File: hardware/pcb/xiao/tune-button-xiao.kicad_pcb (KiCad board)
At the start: 2 copper layers, 46 x 67 mm, 18 parts, among them J1 XIAO left, J2 XIAO right, J3 LiPo, J4 to XIAO BAT, SW1 MX switch, SW2 MX switch, SW3 MX switch, SW4 MX switch

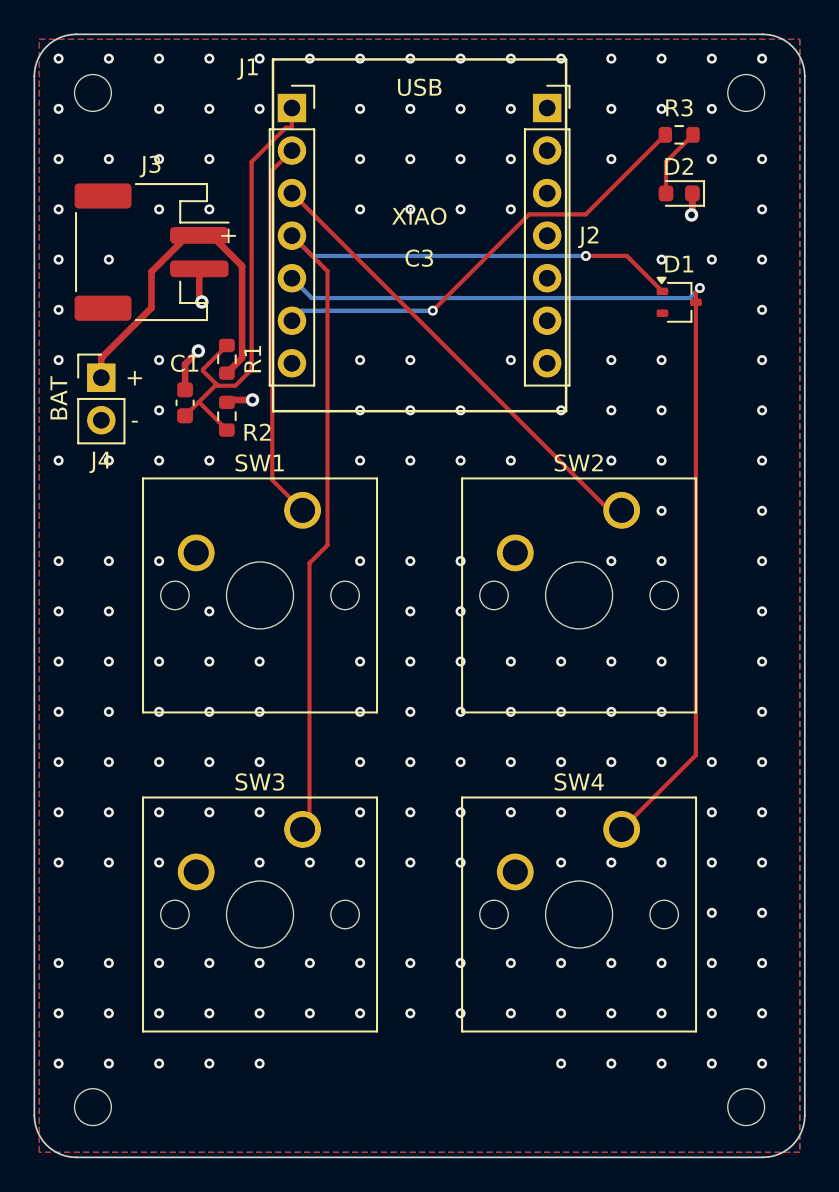
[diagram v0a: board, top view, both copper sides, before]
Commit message: pcb: fixes from the second DFM audit and visual review
- JLC BOM: no designator ranges (KiCad wrote R5-R7, so the CPL lost R5/R6/R7); fab_jlc.py now
  refuses a BOM part with no placement.
- Stitching vias kept off SMD pad openings (two were in the module ground pad's paste).
- Logo drawn as rows at the stroke pitch with caps inset, so gaps keep their size; 15 mm wide.
- Labels only where their own part is the nearest body (R13 and U4 were ambiguous).
- Battery + marks off the pads; USB-C slot paste overprinted 0.2 mm; footprint silk >= 0.15 mm.
- C3 board 70.1 mm long so the USB-C legs clear the switch housings by 0.3 mm.
- Stop tracking __pycache__.
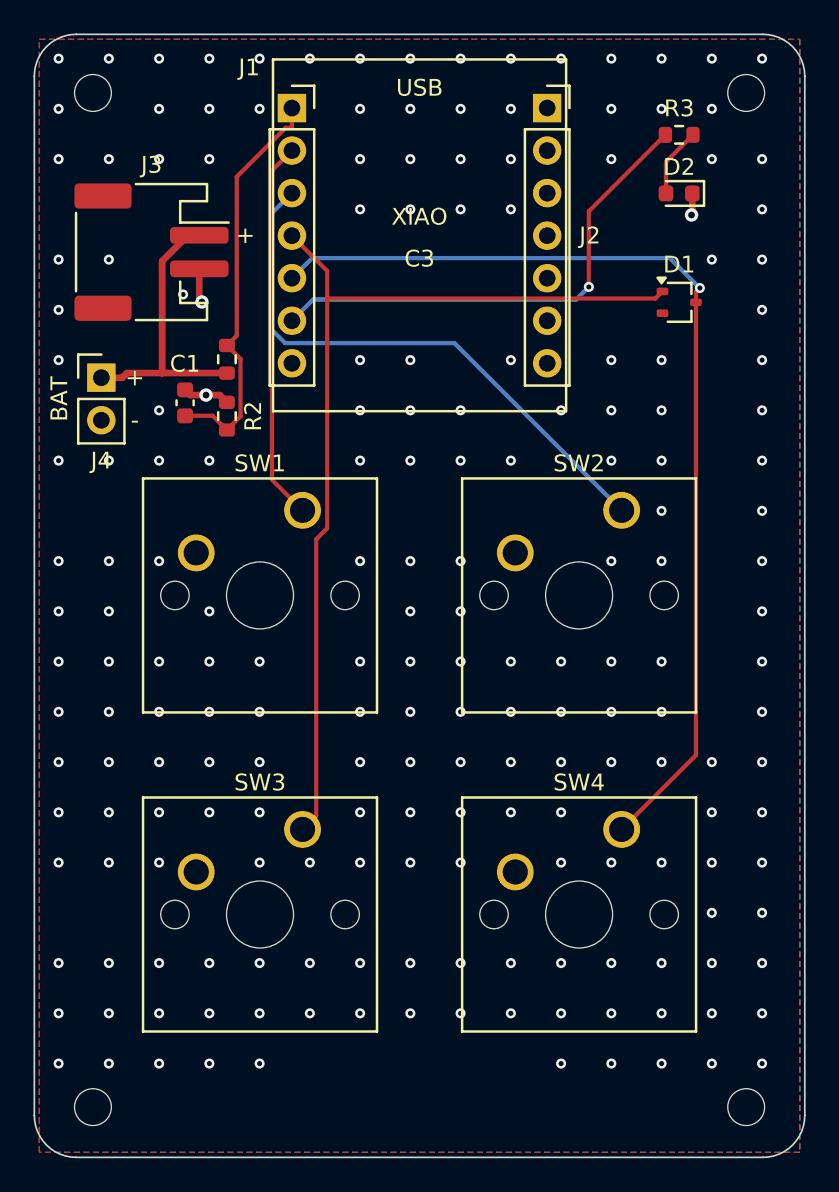
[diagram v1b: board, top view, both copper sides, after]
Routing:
- net K2: track 27.5 -> 34.0 mm
- net VBAT: track 21.4 -> 17.2 mm
- net K3: track 60.4 -> 57.1 mm, vias 1 -> 0
- net VBAT_SENSE: track 27.6 -> 24.6 mm
- net LED: track 26.9 -> 29.5 mm
- net GND: track 7.59 -> 6.16 mm, vias 207 -> 202

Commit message: pcb (c3): fixes from the second simulation pass
- C1 4.7u -> 10u 0805 (C15850, Basic): with R13, plug-in ringing on low-resistance cables peaks
  around 5.6 V instead of 6.1 V (RT9080 absolute max 6.5 V).
- D4, a 1N5819WS across Q1: in the ~3-5 ms after unplugging, before Q1 turns on, the cell feeds
  VSYS through 0.35 V rather than the body diode's 0.6 V, so a Wi-Fi burst there stays above
  brown-out at a 3.4 V cell.
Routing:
- net K3: track 57.1 -> 61.6 mm, vias 0 -> 1
- net LED: track 29.5 -> 27.0 mm
- net GND: track 6.16 -> 7.60 mm, vias 202 -> 211
- net K4: track 59.9 -> 58.7 mm
- net VBAT_SENSE: track 24.6 -> 25.3 mm
- net K1: track 22.7 -> 22.2 mm

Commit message: pcb: black solder mask, white legend in the board stackup
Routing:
- net K2: track 33.9 -> 27.5 mm
- net GND: track 7.60 -> 6.16 mm, vias 211 -> 205
- net K3: track 61.6 -> 60.7 mm
- net VBAT_SENSE: track 25.3 -> 24.6 mm
- net K4: track 58.7 -> 59.4 mm
- net K1: track 22.2 -> 22.7 mm

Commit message: pcb: third DFM audit and visual fixes
- JLCJLCJLCJLC order-number marker (C3 electronics side, XIAO back); README: black mask,
  lead-free HASL, 'Specify a location', overhang remark.
- Logo scaled by the mark's own extent (15 mm printed, was 12.4); vias 1 mm clear of back art.
- D1/D3 labels merged into the back text; keycaps are label obstacles on front-key boards.
- USB-C slot paste overprint 0.12 mm (0.15 mm stencil web).
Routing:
- net K2: track 27.5 -> 32.5 mm
- net VBAT_SENSE: track 24.6 -> 29.1 mm
- net K3: track 60.7 -> 65.1 mm, vias 1 -> 0
- net VBAT: track 17.2 -> 21.4 mm
- net GND: track 6.16 -> 7.87 mm, vias 205 -> 198
- net LED: track 27.0 -> 26.9 mm, vias 1 -> 0
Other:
- board text added: "JLCJLCJLCJLC"

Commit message: pcb (c3): fixes from the third simulation pass
- C1's damping resistor 1 -> 0.5 ohm (R13 + R14, two Basic 1 ohm): with 1 ohm a stiff 5.5 V
  source and no cell rang VSYS to 6.8 V, past the RT9080's 6.5 V; 0.47 ohm simulated under 6.4 V
  on every cable corner.
- R5 10k -> 3.3k: the bigger C1 had stretched the unplug gap to 13-28 ms; ~5-7 ms again.
- README: D4's hot reverse leakage means the cell's protection board is the overcharge backstop.
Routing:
- net VBAT: track 21.4 -> 25.6 mm
- net K3: track 65.1 -> 61.3 mm
- net VBAT_SENSE: track 29.1 -> 26.6 mm
- net GND: track 7.87 -> 9.92 mm, vias 198 -> 183

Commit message: pcb: fourth DFM audit fixes
- route.py stitches with pour islands kept, then removes the ones still unconnected: a 44 mm2 pocket
  of back GND fenced in by tracks near the module was being dropped before it could get a via.
- Zero-length track segments pruned.
- Logo: gaps narrower than the 0.15 mm legend limit are opened to 0.15 rather than left to fill.
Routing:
- net VBAT: track 25.6 -> 17.2 mm
- net K3: track 61.3 -> 58.0 mm
- net GND: track 9.92 -> 7.65 mm, vias 183 -> 198
- net K2: track 32.5 -> 34.0 mm
- net VBAT_SENSE: track 26.6 -> 25.2 mm
- net K1: track 23.4 -> 22.7 mm
- net LED: vias 0 -> 1

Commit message: pcb: fixes from the fourth simulation pass
- C3: R13/R14 (plug-in damping) are 1206, not 0603. Each takes a ~35 W,
  ~50 uJ pulse per plug-in from a stiff source, about twice an 0603's
  repetitive pulse rating. Moved flat above U4; C1 nudged down.
- XIAO: D1 is a 1N4148WS, not a BAT54W. A Schottky's reverse leakage
  dragged K4 low while K3 was held, from about 60 C.
- R5 comment: the unplug gap is 5-8 ms, up to ~15 ms at tolerance extremes.
- wiring.md: the divider holds GPIO2 below the high threshold; it doesn't
  select the boot mode on the C3, so that is fine.
- README: the firmware pin map doesn't match either board yet, and a low
  cell sags the C3 rail on Wi-Fi-sized bursts.
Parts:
- D1: value BAT54W -> 1N4148WS; footprint Package_TO_SOT_SMD:SOT-323_SC-70 -> Diode_SMD:D_SOD-323
- turned D1 to 90 degrees
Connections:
- D1 pad 1: K3 -> K4
- D1 pad 2: unconnected-(D1-NC-Pad2) -> K3
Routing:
- net K3: track 58.0 -> 64.5 mm, vias 0 -> 1
- net K4: track 59.4 -> 56.3 mm
- net K2: track 34.0 -> 32.5 mm
- net GND: track 7.65 -> 6.16 mm, vias 198 -> 201
- net LED: vias 1 -> 0

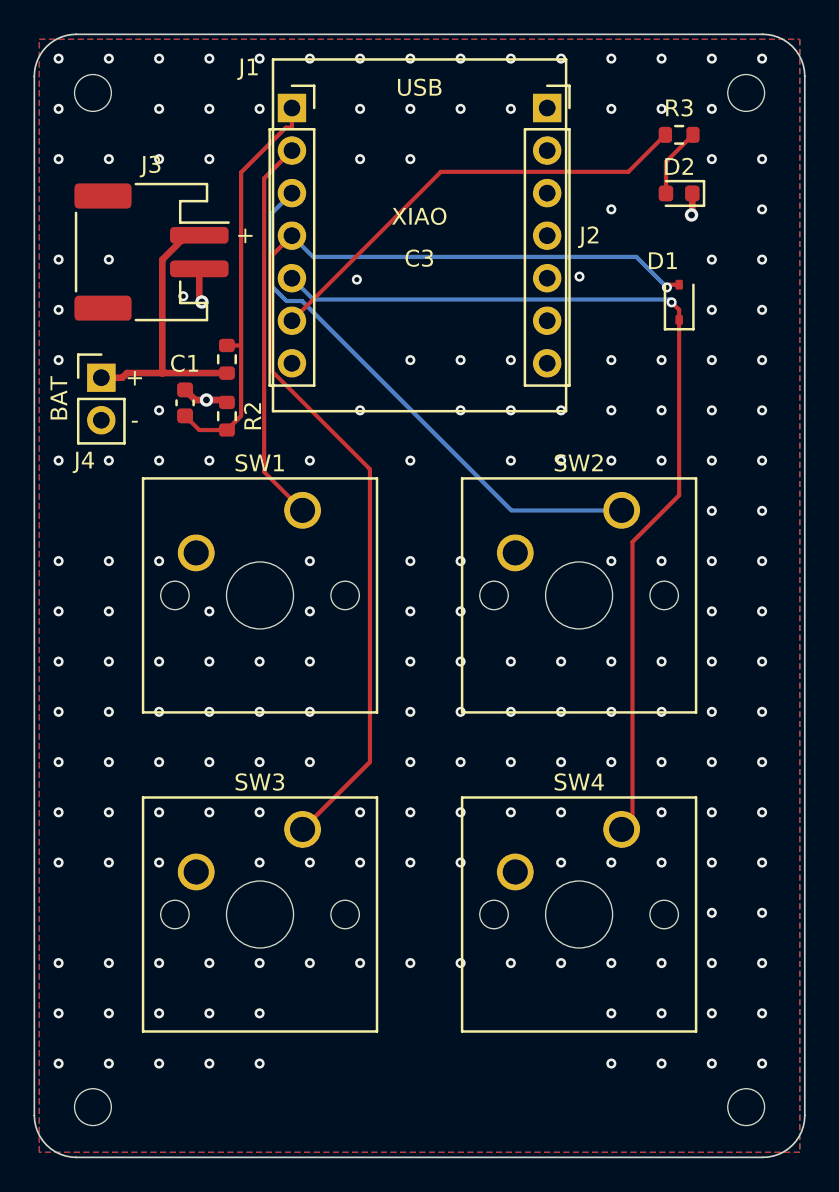
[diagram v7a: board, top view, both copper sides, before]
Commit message: pcb: fixes from the fifth audit
- XIAO D1: LCSC C2128 (Changjing 1N4148WS, Basic), so it appears in the JLC
  BOM/CPL. Its VF max of 0.715 V at 1 mA is what the K4 press needs to read
  low at -20 C; the README says so. Hand-soldering footprint, as that board is.
- Labels: a label must be nearer its own part than any other by 0.25 mm,
  measured edge to edge (it was centre to body). C1's label passes that and
  stays beside C1; U4's, which the first try at this rule hid, is placed.
- route.py drops exactly repeated track segments from the saved board
  (removing them through pcbnew's bindings crashes it later in the run).
- variant_xiao docstring no longer says Schottky.
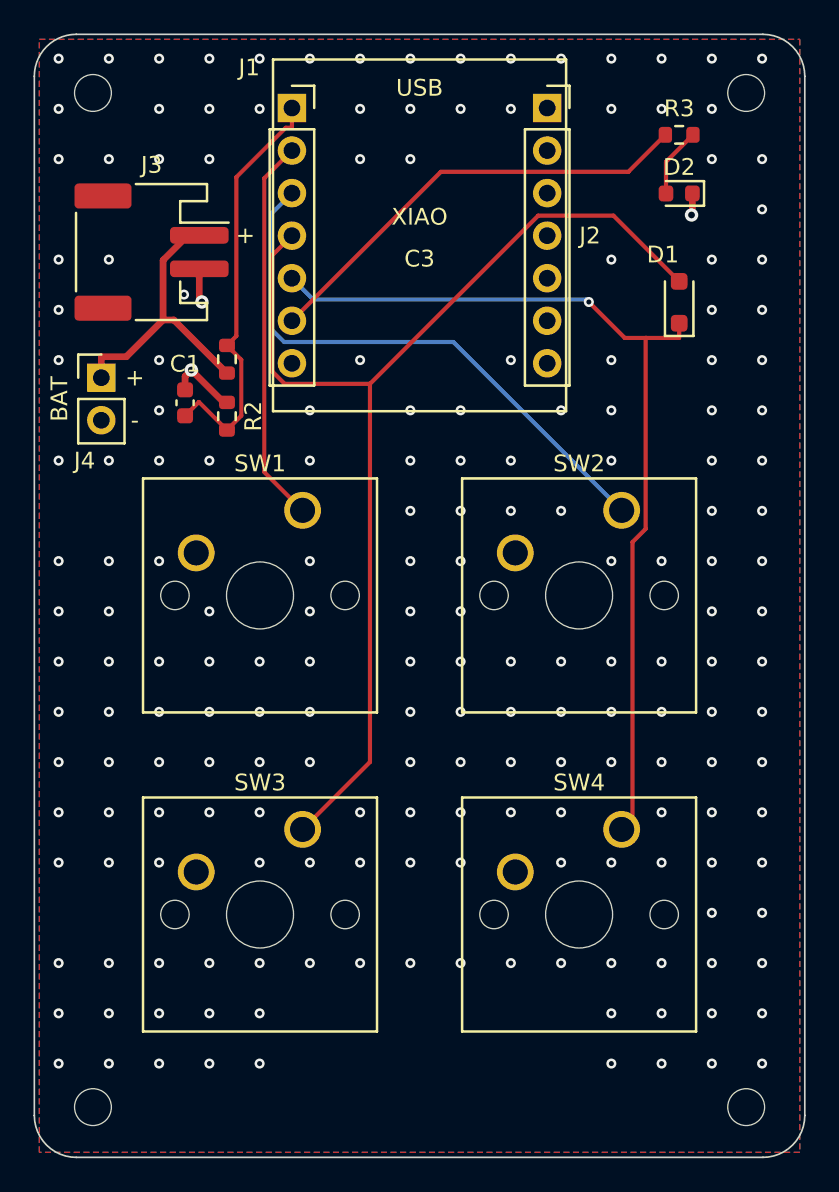
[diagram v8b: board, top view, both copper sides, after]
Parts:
- D1: footprint Diode_SMD:D_SOD-323 -> Diode_SMD:D_SOD-323_HandSoldering
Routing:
- net K3: track 64.5 -> 67.3 mm, vias 1 -> 0
- net K2: track 32.5 -> 34.0 mm
- net GND: track 6.16 -> 7.62 mm, vias 201 -> 200
- net K4: track 56.3 -> 55.4 mm
- net VBAT_SENSE: track 24.7 -> 25.3 mm
